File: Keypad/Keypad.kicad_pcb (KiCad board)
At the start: 2 copper layers, 50 x 35 mm, 15 parts, among them J1 locked, SW1 TL1240GQ1JCLR, SW2 TL1240GQ1JCLR, SW3 TL1240GQ1JCLR, SW4 TL1240GQ1JCLR, SW5 TL1240GQ1JCLR, SW6 TL1240GQ1JCLR

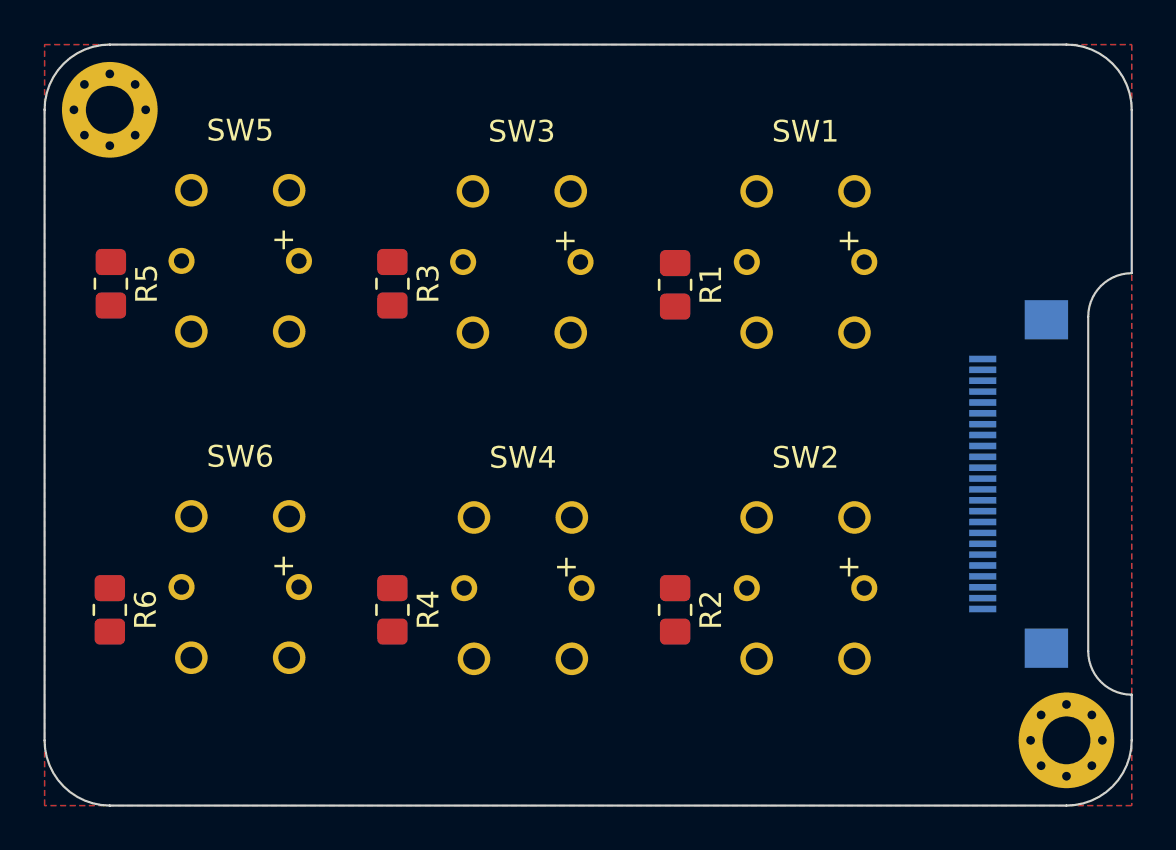
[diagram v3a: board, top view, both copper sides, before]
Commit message: Routes keypad
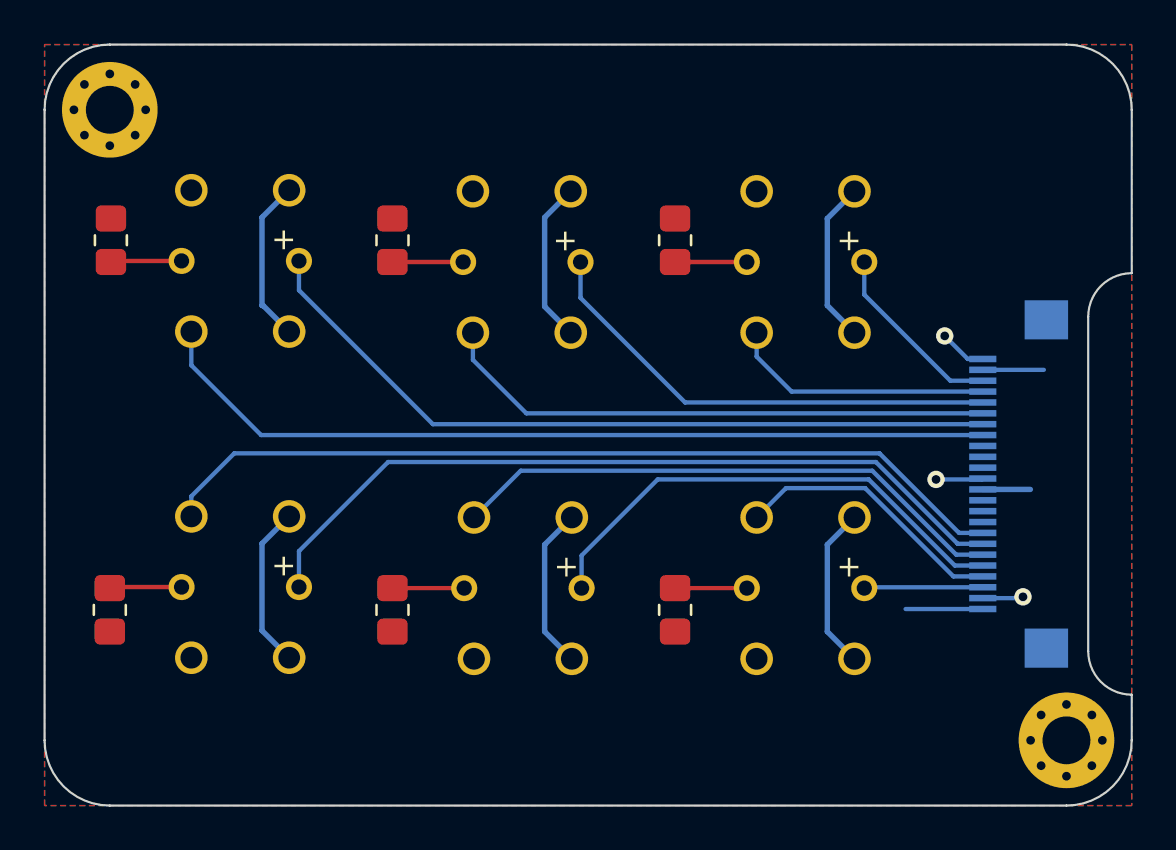
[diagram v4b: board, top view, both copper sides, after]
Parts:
- moved R1 2.05 mm to (149.0, 89.0), turned to 90 degrees
- moved R3 2.00 mm to (136.0, 89.0), turned to 90 degrees
- moved R5 2.00 mm to (123.0, 89.0), turned to 90 degrees
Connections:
- J1 pad 4: unconnected-(J1-IO22) -> SW_1
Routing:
- net +3V3: track 0.00 -> 53.8 mm
- net SW_6: track 0.00 -> 39.7 mm
- net SW_5: track 0.00 -> 39.3 mm
- net LED_6: track 0.00 -> 36.4 mm
- net LED_5: track 0.00 -> 35.4 mm
- net SW_4: track 0.00 -> 25.9 mm
- net SW_3: track 0.00 -> 25.7 mm
- net LED_4: track 0.00 -> 23.0 mm
- net LED_3: track 0.00 -> 22.1 mm
- net SW_2: track 0.00 -> 12.6 mm
- net SW_1: track 0.00 -> 12.2 mm
- net LED_1: track 0.00 -> 8.59 mm
- net GND: track 0.00 -> 6.23 mm, vias 0 -> 3
- net LED_2: track 0.00 -> 5.47 mm
- net Net-(SW6--): track 0.00 -> 3.32 mm
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
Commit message: Flips buttons on keypad
The keypad will have the same orientation as the Sensor board (with the
FFC connector on top). The buttons will be on the same side as the
connector.
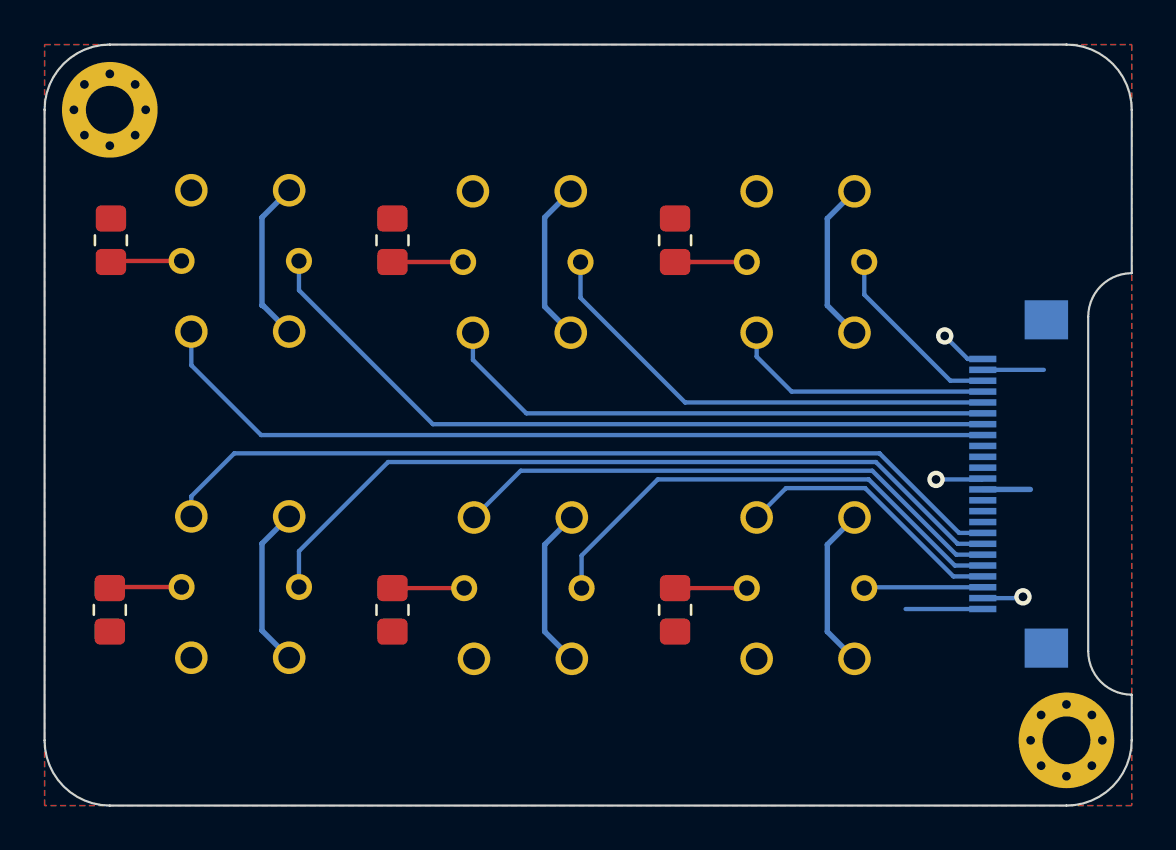
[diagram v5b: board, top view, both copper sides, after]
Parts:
- SW1, SW2, SW3, SW4, SW5, SW6: moved to B.Cu
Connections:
- SW1 pad 3: unconnected-(SW1-Pad3) -> SW_1
- SW1 pad 4: SW_1 -> unconnected-(SW1-Pad4)
- SW2 pad 3: SW_2 -> unconnected-(SW2-Pad3)
- SW2 pad 4: unconnected-(SW2-Pad4) -> SW_2
- SW3 pad 3: unconnected-(SW3-Pad3) -> SW_3
- SW3 pad 4: SW_3 -> unconnected-(SW3-Pad4)
- SW4 pad 3: SW_4 -> unconnected-(SW4-Pad3)
- SW4 pad 4: unconnected-(SW4-Pad4) -> SW_4
- SW5 pad 3: unconnected-(SW5-Pad3) -> SW_5
- SW5 pad 4: SW_5 -> unconnected-(SW5-Pad4)
- SW6 pad 3: SW_6 -> unconnected-(SW6-Pad3)
- SW6 pad 4: unconnected-(SW6-Pad4) -> SW_6

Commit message: Moves buttons a bit further away from screws
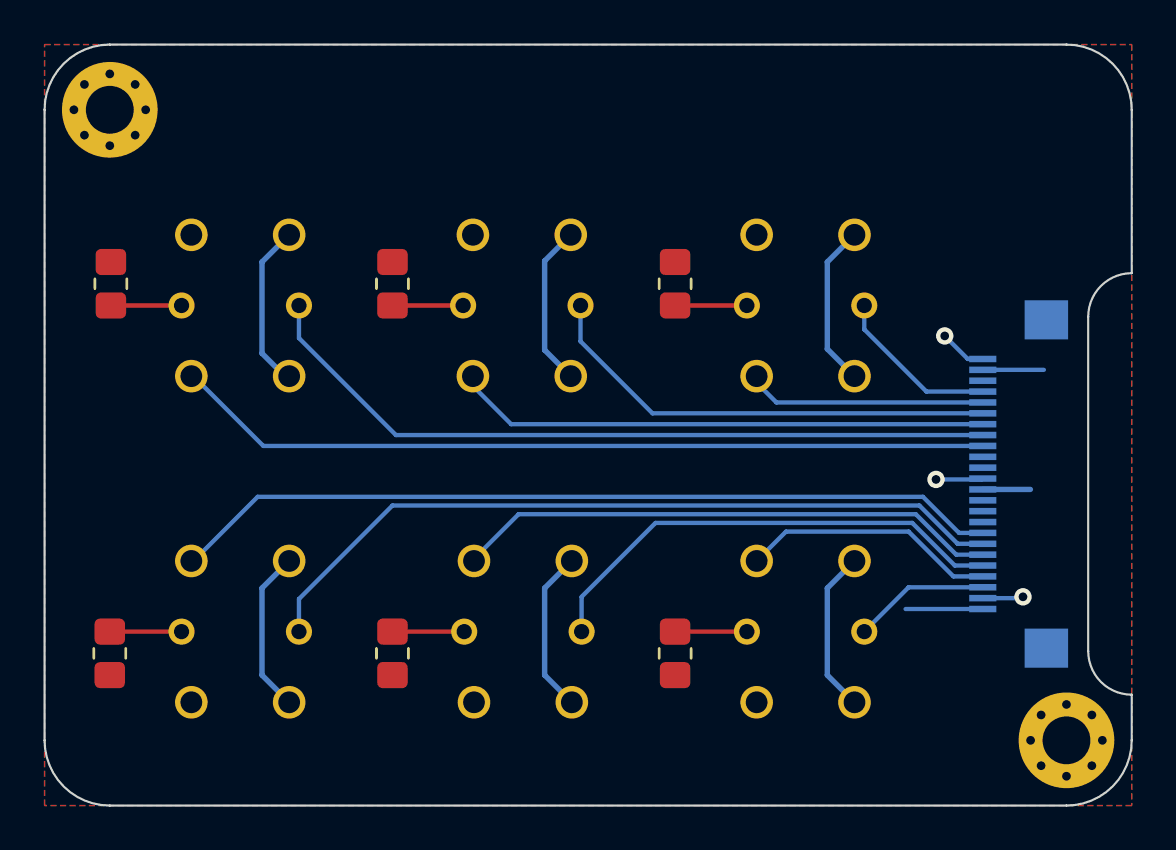
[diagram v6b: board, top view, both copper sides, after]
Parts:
- moved SW5 2.05 mm to (129.0, 92.0)
- moved SW6 2.05 mm to (129.0, 107.0)
- moved R1 2.00 mm to (149.0, 91.0)
- moved R2 2.00 mm to (149.0, 108.0)
- moved R3 2.00 mm to (136.0, 91.0)
- moved R4 2.00 mm to (136.0, 108.0)
- moved R5 2.00 mm to (123.0, 91.0)
- moved R6 2.00 mm to (123.0, 108.0)
- moved SW1 2.00 mm to (155.0, 92.0)
- moved SW2 2.00 mm to (155.0, 107.0)
- moved SW3 2.00 mm to (141.9, 92.0)
- moved SW4 2.00 mm to (142.0, 107.0)
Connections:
- J1 pad 3: LED_1 -> unconnected-(J1-IO23)
- J1 pad 4: SW_1 -> LED_1
- J1 pad 5: LED_3 -> SW_1
- J1 pad 6: SW_3 -> LED_3
- J1 pad 7: LED_5 -> SW_3
- J1 pad 8: SW_5 -> LED_5
- J1 pad 9: unconnected-(J1-IO17) -> SW_5
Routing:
- net SW_5: track 39.3 -> 37.7 mm
- net SW_6: track 39.7 -> 38.3 mm
- net SW_3: track 25.7 -> 24.6 mm
- net SW_1: track 12.2 -> 11.1 mm
- net LED_6: track 36.4 -> 35.5 mm
- net LED_1: track 8.59 -> 7.73 mm
- net LED_2: track 5.47 -> 6.29 mm
- net SW_2: track 12.6 -> 11.8 mm
- net LED_4: track 23.0 -> 22.3 mm
- net SW_4: track 25.9 -> 25.1 mm
- net LED_3: track 22.1 -> 21.5 mm
- net LED_5: track 35.4 -> 34.8 mm

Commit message: Adds gameover logo and revision number to keypad PCB
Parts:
- added Ref**: Val**, GameOver:logo_fcu, B.Cu at (145.0, 84.0)
- added kibuzzard-6290844C: G***, kibuzzard-6290844C, F.Cu at (122.0, 97.0)

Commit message: Fixes logo reference in keypad schematics
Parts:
- removed Ref**: Val**, GameOver:logo_fcu
- added LOGO1: GameOver_logo, GameOver:logo_fcu, B.Cu at (145.0, 84.0)
